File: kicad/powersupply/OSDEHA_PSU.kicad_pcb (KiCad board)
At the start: 2 copper layers, 239.3 x 78.3 mm, 104 parts, among them J1 340 VAC / 220 mA, J2 340 VAC / 220 mA, J3 420 VAC / 75 mA, J4 9 VAC / 4.5 A, J5 Stator bias, J6 HV-L, J7 HV-R, J8 HEATERS-LEFT, J9 HEATERS-RIGHT, K1 RT424006, Q1 BD138, Q10 BC550, Q11 LND150, Q12 LND150, Q13 NTHL1000N170M1, Q14 BC550, Q2 10M90S, Q3 LND150, Q4 LND150, Q5 NTHL1000N170M1, Q6 BC550, Q7 LND150, Q8 LND150, Q9 NTHL1000N170M1, U1 LM1085-ADJ, U2 NE555P

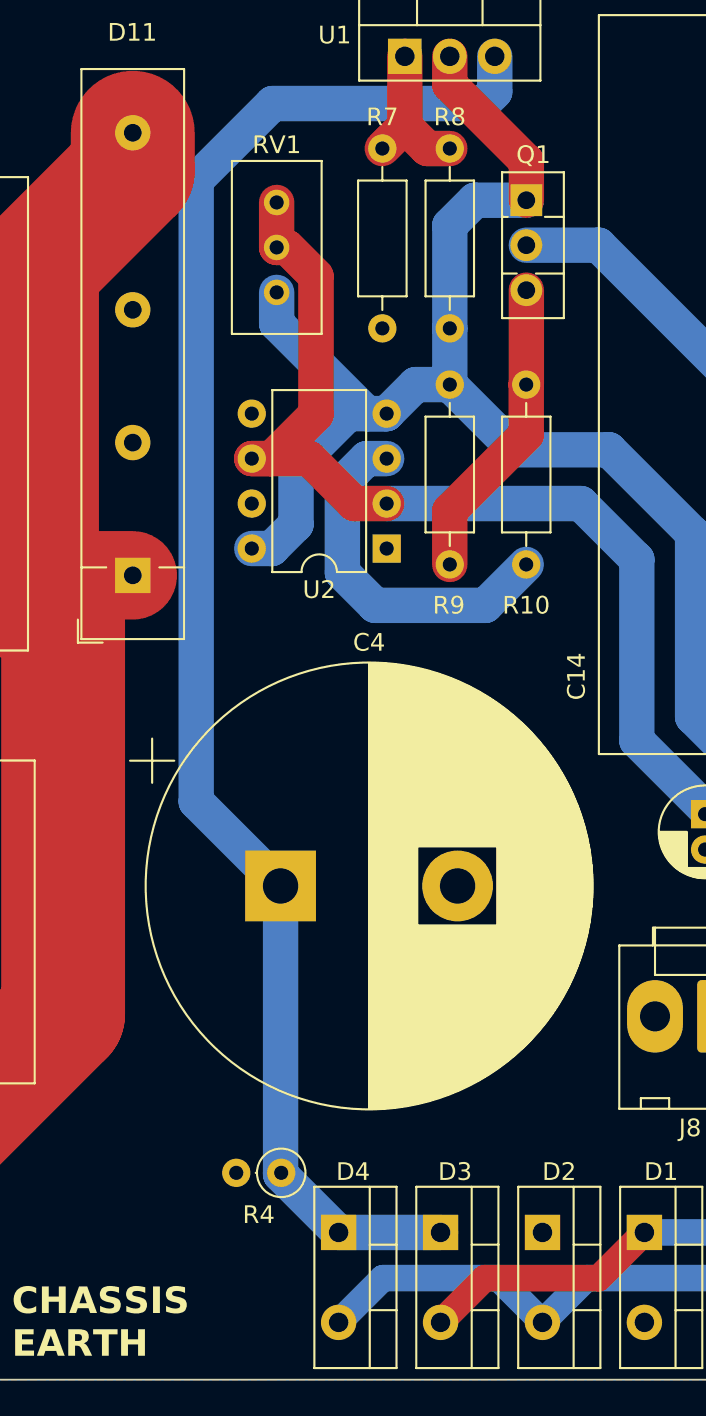
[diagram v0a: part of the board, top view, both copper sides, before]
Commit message: fixed D2 polarity on PCB. Increased size of pads and holes for rectifier bridge in ground loop breaker.
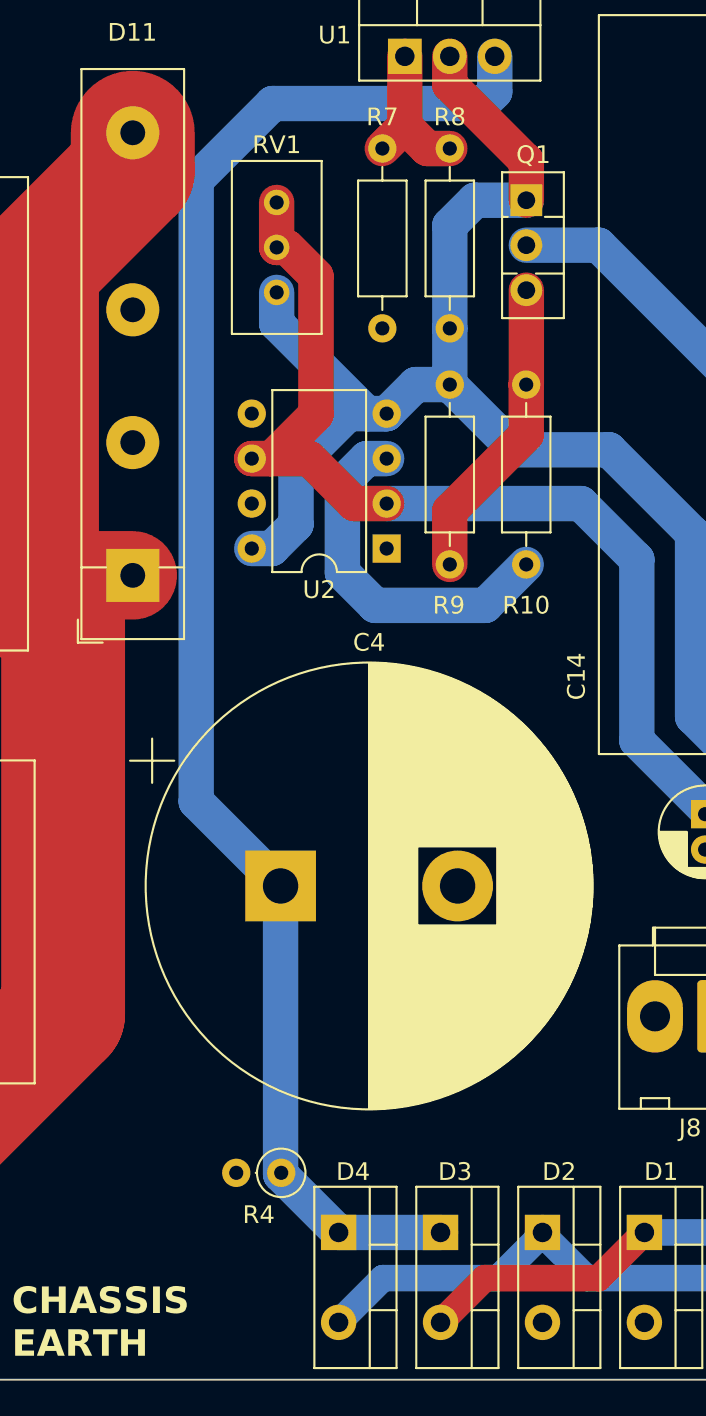
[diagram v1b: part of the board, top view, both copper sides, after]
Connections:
- D2 pad 1: GND -> Net-(D2-K)
- D2 pad 2: Net-(D2-A) -> GND
- D4 pad 2: Net-(D2-A) -> Net-(D2-K)
- J4 pad 1: Net-(D2-A) -> Net-(D2-K)
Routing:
- net Net-(D2-K): track 0.00 -> 28.3 mm
- net Net-(D2-A): track 28.2 -> 0.00 mm

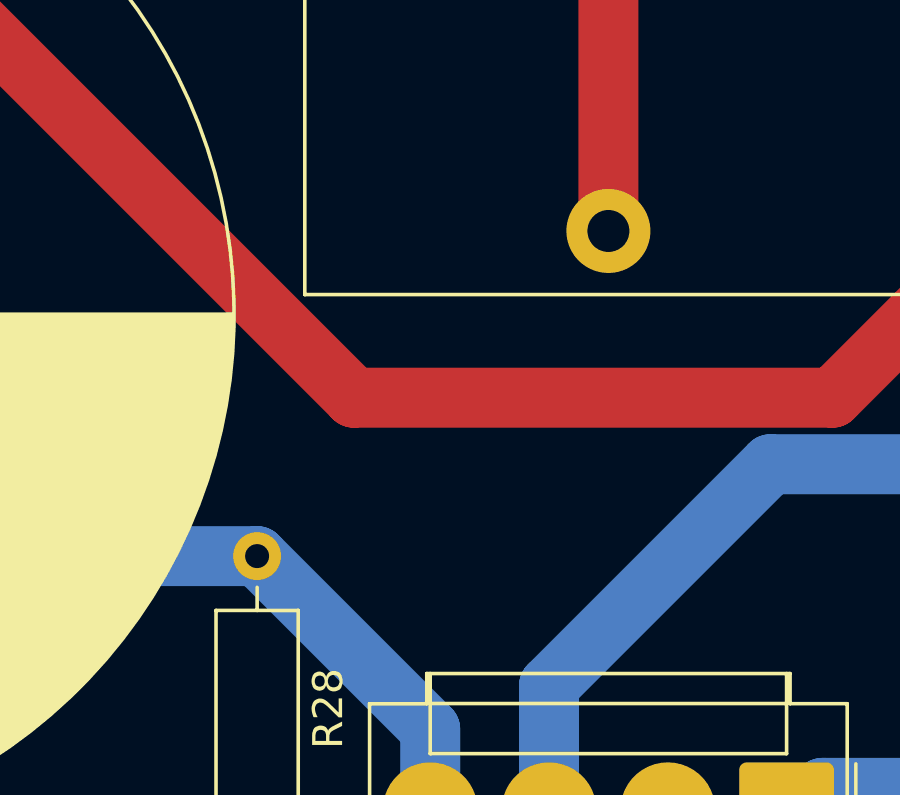
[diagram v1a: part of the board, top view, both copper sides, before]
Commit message: add vias for missing link between ground fills/zones
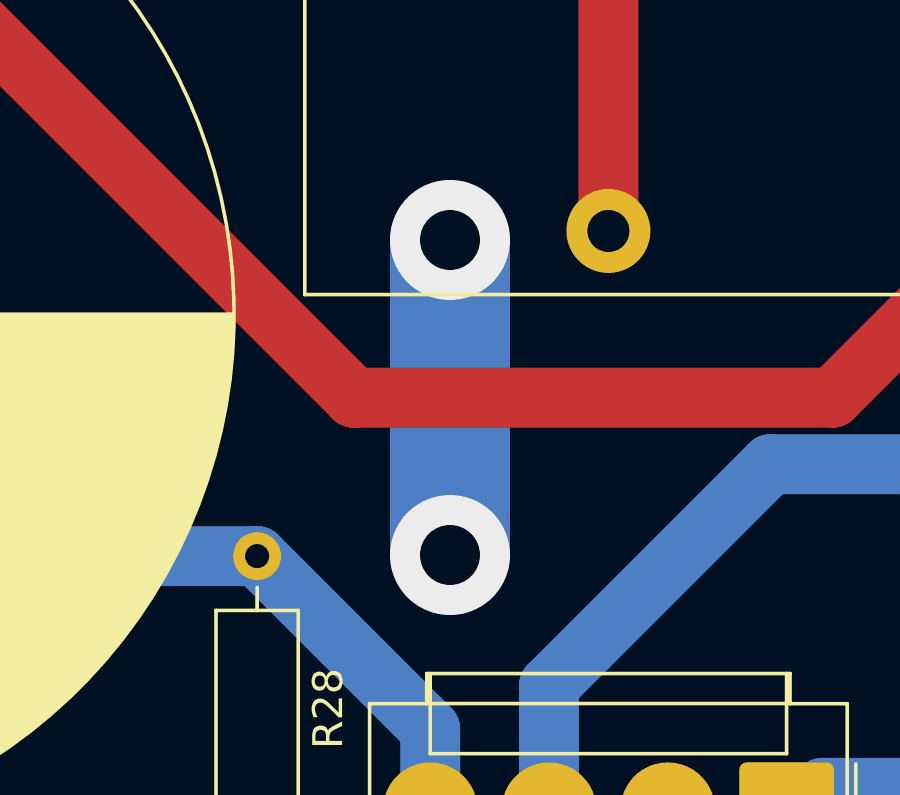
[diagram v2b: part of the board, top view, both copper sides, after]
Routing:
- net GND: track 5.71 -> 16.2 mm, vias 2 -> 4
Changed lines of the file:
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@@
 		(net 1)
+	)
+	(via blind
+		(at 139.5 129.5)
+		(size 4)
+		(drill 2)
+		(layers "F.Cu" "B.Cu")
+		(net 2)
 	)
 	(via
@@
 		(size 2)
 		(drill 1)
+		(layers "F.Cu" "B.Cu")
+		(net 2)
+	)
+	(via blind
+		(at 139.5 119)
+		(size 4)
+		(drill 2)
 		(layers "F.Cu" "B.Cu")
 		(net 2)
@@
 		(layer "B.Cu")
 		(net 2)
+	)
+	(segment
+		(start 139.5 129.5)
+		(end 139.5 119)
+		(width 4)
+		(layer "B.Cu")
+		(net 2)

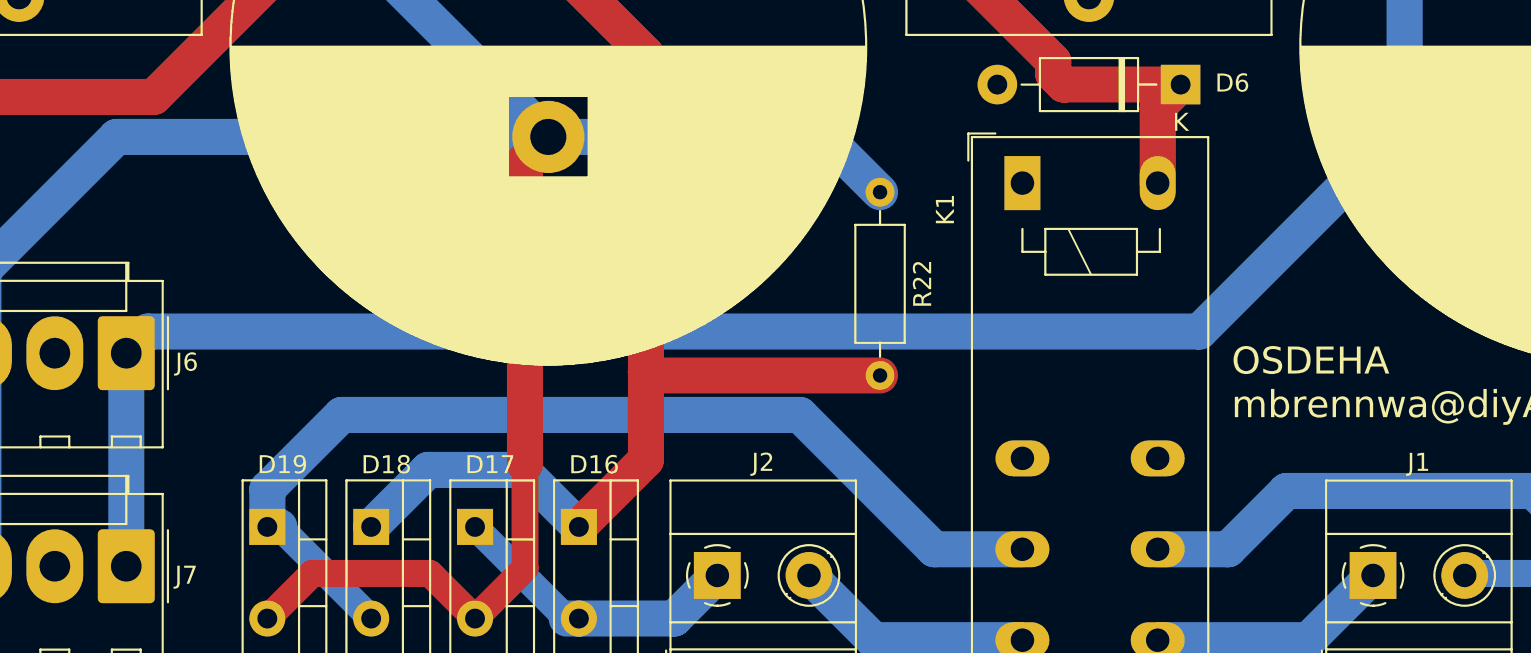
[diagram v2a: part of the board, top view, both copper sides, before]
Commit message: added additional mounting hole
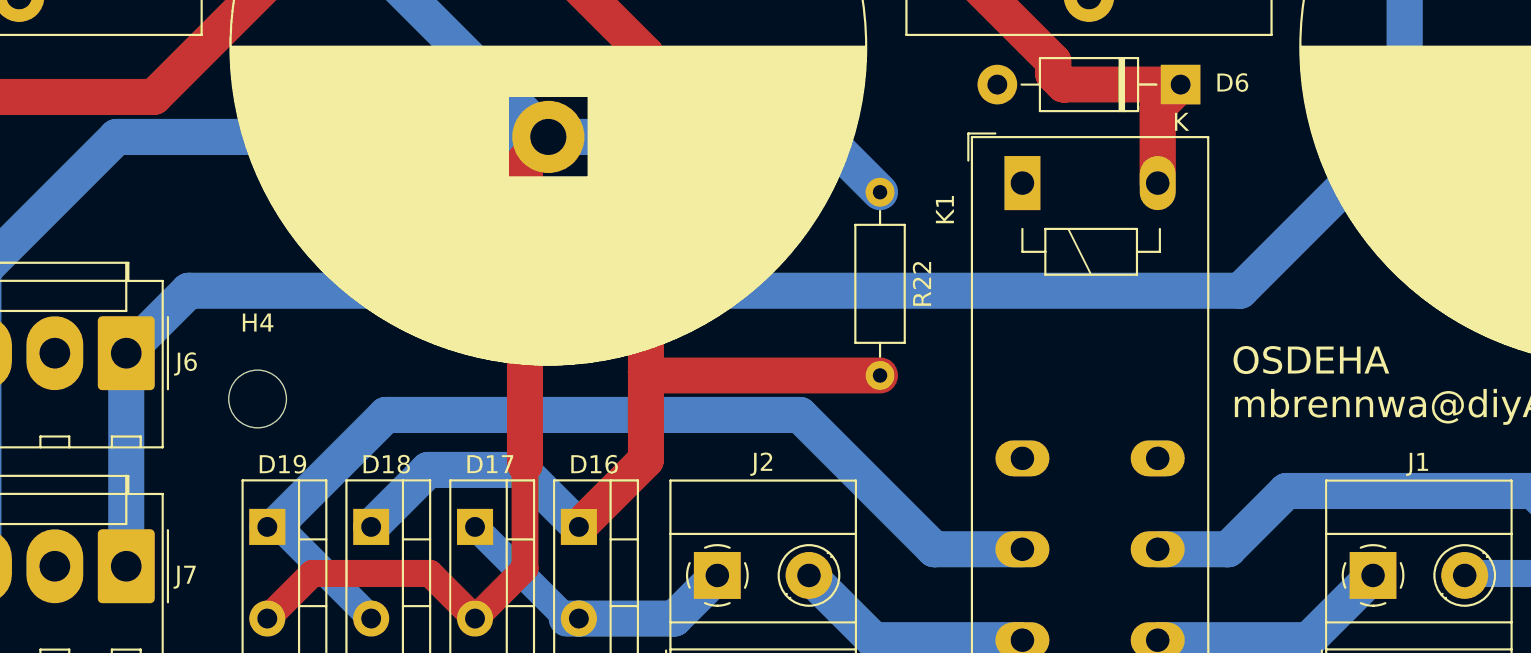
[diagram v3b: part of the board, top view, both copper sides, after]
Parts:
- added H4: MountingHole, MountingHole:MountingHole_3.2mm_M3, F.Cu at (158.0, 141.0)
- R1, R2: value 787k -> 866k
- R18, R24, R30: value 1.5k -> 1k
- R3: value 976k -> 1.1M
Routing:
- net /HV_STABI2/AC2: track 56.6 -> 55.4 mm
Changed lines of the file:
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@@
 			)
 		)
+		(property ki_fp_filters "D*Bridge*32.0x5.6x17.0mm*P10.0mm*P7.5mm*")
+		(sheetname "Root")
+		(sheetfile "OSDEHA_PSU.kicad_sch")
 		(attr through_hole)
 		(fp_line
@@
 			)
 		)
-		(property "Value" "1.5k"
+		(property "Value" "1k"
 			(at 5.08 2.37 90)
 			(layer "F.Fab")
@@
 			)
 		)
-		(property "MPN" "CMF551K5000"
+		(property "MPN" "CMF551K0000"
 			(at 0 0 0)
 			(layer "F.Fab")
@@
 			)
 		)
-		(property "Value" "1.5k"
+		(property "Value" "1k"
 			(at 5.08 2.37 90)
 			(layer "F.Fab")
@@
 			)
 		)
-		(property "MPN" "CMF551K5000"
+		(property "MPN" "CMF551K0000"
 			(at 0 0 0)
 			(layer "F.Fab")
@@
 			)
 		)
-		(property "Value" "1.5k"
+		(property "Value" "1k"
 			(at 5.08 2.37 90)
 			(layer "F.Fab")
@@
 			)
 		)
-		(property "MPN" "CMF551K5000"
+		(property "MPN" "CMF551K0000"
 			(at 0 0 0)
 			(layer "F.Fab")
@@
 			)
 		)
-		(property "Value" "787k"
+		(property "Value" "866k"
 			(at 5.08 2.37 90)
 			(layer "F.Fab")
@@
 			)
 		)
-		(property "MPN" "CMF55787K00"
+		(property "MPN" "CMF55866K00"
 			(at 0 0 0)
 			(layer "F.Fab")
@@
 			)
 		)
-		(property "Value" "976k"
+		(property "Value" "1.1M"
 			(at 5.08 2.37 90)
 			(layer "F.Fab")
@@
 			)
 		)
-		(property "MPN" "CMF55976K00"
+		(property "MPN" "CMF551M1000"
 			(at 0 0 0)
 			(layer "F.Fab")
@@
 			)
 		)
-		(property "Value" "787k"
+		(property "Value" "866k"
 			(at 5.08 2.37 90)
 			(layer "F.Fab")
@@
 			)
 		)
-		(property "MPN" "CMF55787K00"
+		(property "MPN" "CMF55866K00"
 			(at 0 0 0)
 			(layer "F.Fab")
@@
 		)
 	)
+	(footprint "MountingHole:MountingHole_3.2mm_M3"
+		(layer "F.Cu")
+		(at 158 141)
+		(descr "Mounting Hole 3.2mm, no annular, M3")
+		(tags "mounting hole 3.2mm no annular m3")
+		(property "Reference" "H4"
+			(at 0 -4.2 0)
+			(layer "F.SilkS")
+			(effects
+				(font
+					(size 1 1)
+					(thickness 0.15)
+				)
+			)
+		)
+		(property "Value" "MountingHole"
+			(at 0 4.2 0)
+			(layer "F.Fab")
+			(effects
+				(font
+					(size 1 1)
+					(thickness 0.15)
+				)
+			)
+		)
+		(property "Footprint" "MountingHole:MountingHole_3.2mm_M3"
+			(at 0 0 0)
+			(unlocked yes)
+			(layer "F.Fab")
+			(hide yes)
+			(effects
+				(font
+					(size 1.27 1.27)
+				)
+			)
+		)
+		(property "Datasheet" ""
+			(at 0 0 0)
+			(unlocked yes)
+			(layer "F.Fab")
+			(hide yes)
+			(effects
+				(font
+					(size 1.27 1.27)
+				)
+			)
+		)
+		(property "Description" ""
+			(at 0 0 0)
+			(unlocked yes)
+			(layer "F.Fab")
+			(hide yes)
+			(effects
+				(font
+					(size 1.27 1.27)
+				)
+			)
+		)
+		(property ki_fp_filters "MountingHole*")
+		(sheetname "Root")
+		(sheetfile "OSDEHA_PSU.kicad_sch")
+		(attr exclude_from_pos_files)
+		(fp_circle
+			(center 0 0)
+			(end 3.2 0)
+			(stroke
+				(width 0.15)
+				(type solid)
+			)
+			(fill none)
+			(layer "Cmts.User")
+		)
+		(fp_circle
+			(center 0 0)
+			(end 3.45 0)
+			(stroke
+				(width 0.05)
+				(type solid)
+			)
+			(fill none)
+			(layer "F.CrtYd")
+		)
+		(fp_text user "${REFERENCE}"
+			(at 0 0 0)
+			(layer "F.Fab")
+			(effects
+				(font
+					(size 1 1)
+					(thickness 0.15)
+				)
+			)
+		)
+		(pad "" np_thru_hole circle
+			(at 0 0)
+			(size 3.2 3.2)
+			(drill 3.2)
+			(layers "*.Cu" "*.Mask")
+		)
+	)
 	(footprint "Resistor_THT:R_Axial_DIN0207_L6.3mm_D2.5mm_P10.16mm_Horizontal"
 		(layer "F.Cu")
@@
 	)
 	(segment
-		(start 200.399 149.332501)
-		(end 195.509701 149.332501)
+		(start 158.907499 148.092501)
+		(end 158.539 148.092501)
 		(width 2)
 		(layer "B.Cu")
@@
 	)
 	(segment
-		(start 195.509701 149.332501)
-		(end 188.0616 141.8844)
+		(start 200.399 149.332501)
+		(end 195.509701 149.332501)
 		(width 2)
 		(layer "B.Cu")
@@
 	)
 	(segment
-		(start 158.539 146.007)
-		(end 158.539 148.092501)
+		(start 188.0616 141.8844)
+		(end 165.1156 141.8844)
 		(width 2)
 		(layer "B.Cu")
@@
 	)
 	(segment
-		(start 188.0616 141.8844)
-		(end 162.6616 141.8844)
+		(start 165.1156 141.8844)
+		(end 158.907499 148.092501)
 		(width 2)
 		(layer "B.Cu")
@@
 	)
 	(segment
-		(start 162.6616 141.8844)
-		(end 158.539 146.007)
+		(start 195.509701 149.332501)
+		(end 188.0616 141.8844)
 		(width 2)
 		(layer "B.Cu")
@@
 	)
 	(segment
-		(start 151.919901 137.2616)
-		(end 150.72 138.461501)
-		(width 2)
-		(layer "B.Cu")
-		(net 29)
-	)
-	(segment
 		(start 233.2228 106.3752)
 		(end 227.9904 106.3752)
@@
 	(segment
 		(start 221.5896 125.8824)
-		(end 210.2104 137.2616)
+		(end 212.472 135)
 		(width 2)
 		(layer "B.Cu")
@@
 	)
 	(segment
-		(start 221.5896 112.776)
-		(end 221.5896 125.8824)
+		(start 150.72 138.461501)
+		(end 150.72 150.272501)
 		(width 2)
 		(layer "B.Cu")
@@
 	)
 	(segment
-		(start 150.72 138.461501)
-		(end 150.72 150.272501)
+		(start 154.181501 135)
+		(end 150.72 138.461501)
 		(width 2)
 		(layer "B.Cu")
@@
 	)
 	(segment
-		(start 210.2104 137.2616)
-		(end 151.919901 137.2616)
+		(start 212.472 135)
+		(end 154.181501 135)
 		(width 2)
 		(layer "B.Cu")
@@
 		(width 2)
 		(layer "B.Cu")
+		(net 29)
+	)
+	(segment
+		(start 221.5896 112.776)
+		(end 221.5896 125.8824)
+		(width 2)
+		(layer "B.Cu")

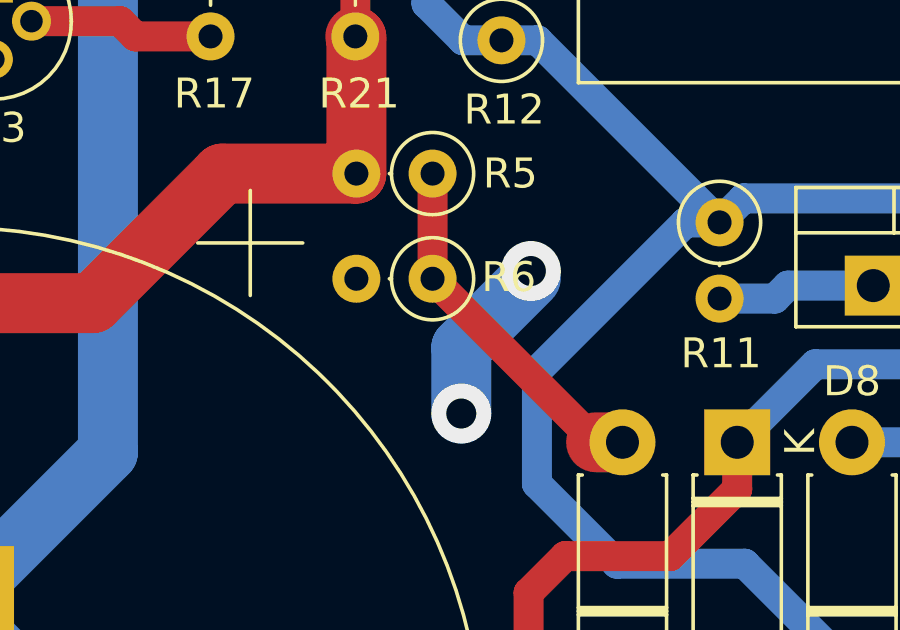
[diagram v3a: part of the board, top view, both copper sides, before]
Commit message: update PSU testing
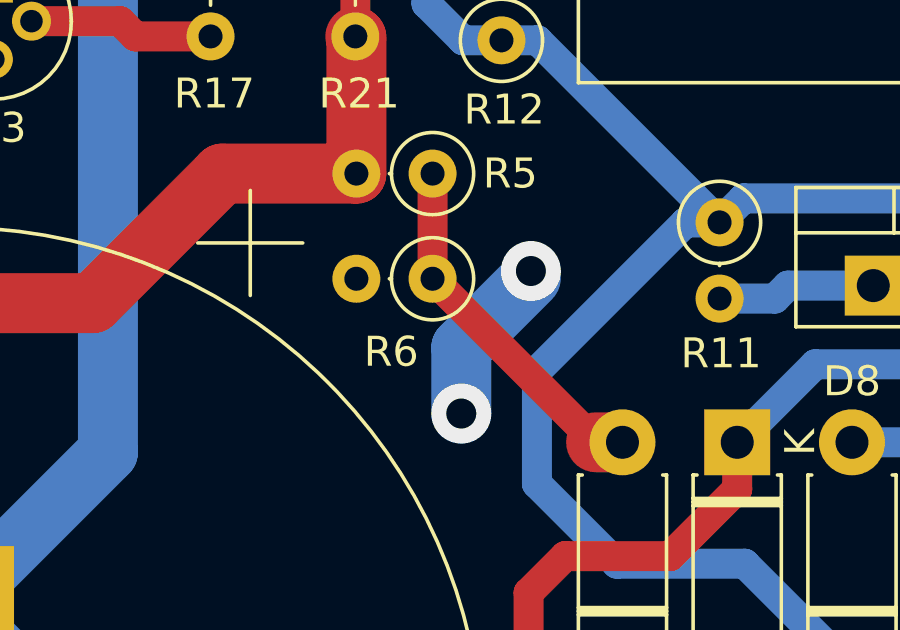
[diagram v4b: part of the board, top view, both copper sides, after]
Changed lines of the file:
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@@
 		(tags "Resistor Axial_DIN0207 series Axial Vertical pin pitch 2.54mm 0.25W = 1/4W length 6.3mm diameter 2.5mm")
 		(property "Reference" "R6"
-			(at -2.54 0.0508 0)
+			(at 1.3772 -2.4376 0)
 			(layer "F.SilkS")
 			(effects

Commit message: modified pin / net labels
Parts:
- R6: value 787k -> 866k
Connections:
- net /HV_STABI1/DC+ renamed /B+
- net /HV_STABI2/DC- renamed /B-
- net /HV_STABI3/DC- renamed /B2-
- net Net-(J5-Pin_1) renamed /BIAS
- net Net-(J8-Pin_1) renamed /H
- C5 pad 2: /HV_STABI1/AC1 -> /ACB+
- D1 pad 1: Net-(D1-K) -> /ACHTR
- D12 pad 2: /HV_STABI1/AC1 -> /ACB+
- D13 pad 1: /HV_STABI1/AC1 -> /ACB+
- D16 pad 2: /HV_STABI2/AC1 -> /ACB-
- D17 pad 1: /HV_STABI2/AC1 -> /ACB-
- D2 pad 1: Net-(D2-K) -> /ACHTR
- D20 pad 2: /HV_STABI3/AC1 -> /ACB2-
- D21 pad 1: /HV_STABI3/AC1 -> /ACB2-
- D22 pad 2: /HV_STABI3/AC2 -> /ACB2-
- D23 pad 1: /HV_STABI3/AC2 -> /ACB2-
- D3 pad 2: Net-(D1-K) -> /ACHTR
- D4 pad 2: Net-(D2-K) -> /ACHTR
- J1 pad 1: Net-(J1-Pin_1) -> /ACB+
- J1 pad 2: /HV_STABI1/AC1 -> /ACB+
- J2 pad 1: /HV_STABI2/AC1 -> /ACB-
- J2 pad 2: Net-(J2-Pin_2) -> /ACB-
- J3 pad 1: /HV_STABI3/AC2 -> /ACB2-
- J3 pad 2: /HV_STABI3/AC1 -> /ACB2-
- J4 pad 1: Net-(D2-K) -> /ACHTR
- J4 pad 2: Net-(D1-K) -> /ACHTR
- K1 pad 14: Net-(J2-Pin_2) -> /ACB-
- K1 pad 24: Net-(J1-Pin_1) -> /ACB+
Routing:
- net /ACB+: track 0.00 -> 69.7 mm
- net /ACB2-: track 0.00 -> 64.3 mm
- net /HV_STABI1/AC1: track 56.3 -> 0.00 mm
- net /ACHTR: track 0.00 -> 55.9 mm
- net /HV_STABI3/AC2: track 47.5 -> 0.00 mm
- net /ACB-: track 0.00 -> 29.8 mm
- net Net-(D2-K): track 28.3 -> 0.00 mm
- net Net-(D1-K): track 27.6 -> 0.00 mm
- net /HV_STABI3/AC1: track 16.8 -> 0.00 mm
- net /HV_STABI2/AC1: track 16.5 -> 0.00 mm
- net Net-(J1-Pin_1): track 13.4 -> 0.00 mm
- net Net-(J2-Pin_2): track 13.3 -> 0.00 mm
